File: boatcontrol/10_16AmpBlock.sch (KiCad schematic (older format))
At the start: 15 parts, among them U6101 ULN2803A

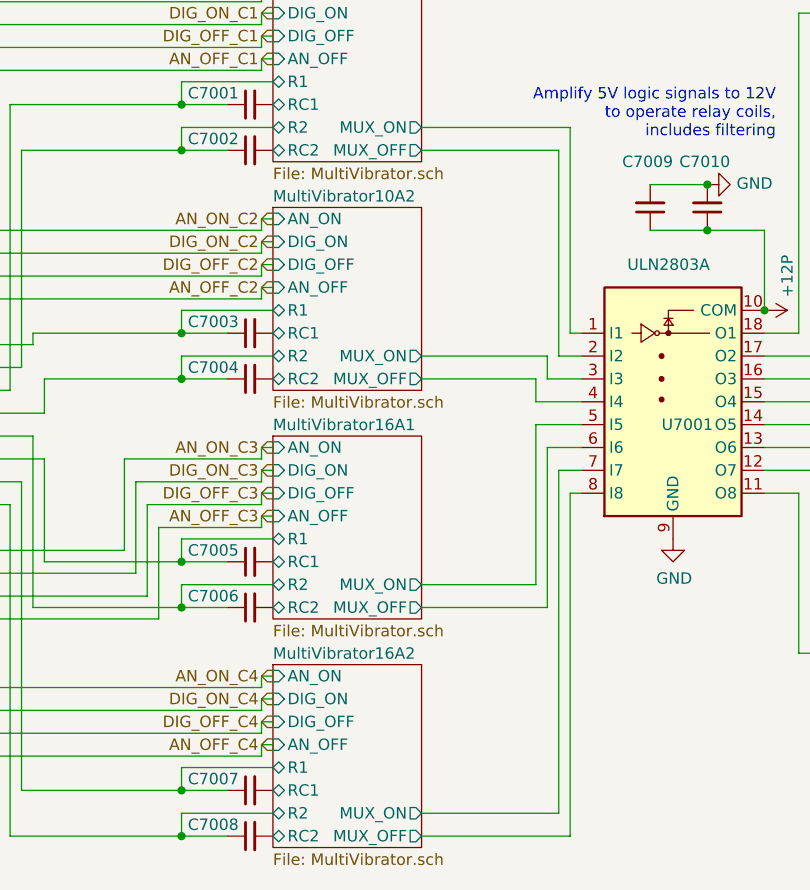
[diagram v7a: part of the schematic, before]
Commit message: Add xors on input
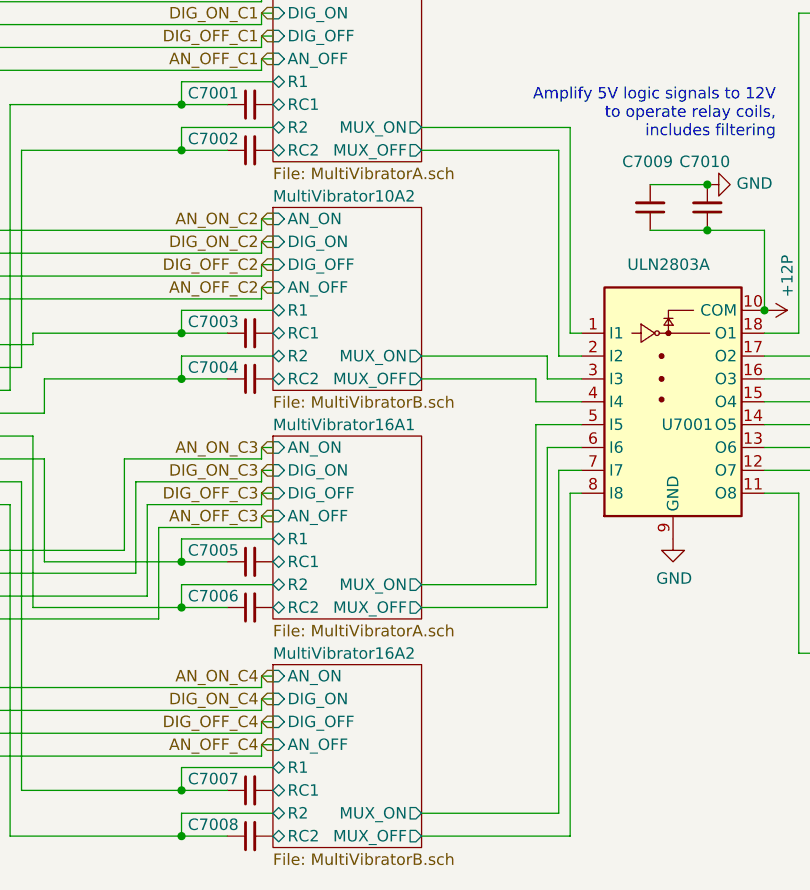
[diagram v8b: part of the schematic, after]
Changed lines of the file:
@@
 U 604747CD
 F0 "MultiVibrator10A1" 50
-F1 "MultiVibrator.sch" 50
+F1 "MultiVibratorA.sch" 50
 F2 "DIG_OFF" I L 4750 2200 50
 F3 "AN_OFF" I L 4750 2300 50
@@
 U 604747E7
 F0 "MultiVibrator10A2" 50
-F1 "MultiVibrator.sch" 50
+F1 "MultiVibratorB.sch" 50
 F2 "DIG_OFF" I L 4750 3200 50
 F3 "AN_OFF" I L 4750 3300 50
@@
 U 604747F3
 F0 "MultiVibrator16A1" 50
-F1 "MultiVibrator.sch" 50
+F1 "MultiVibratorA.sch" 50
 F2 "DIG_OFF" I L 4750 4200 50
 F3 "AN_OFF" I L 4750 4300 50
@@
 U 604747FF
 F0 "MultiVibrator16A2" 50
-F1 "MultiVibrator.sch" 50
+F1 "MultiVibratorB.sch" 50
 F2 "DIG_OFF" I L 4750 5200 50
 F3 "AN_OFF" I L 4750 5300 50
@@
 AR Path="/D16552B4/5FA17F86/602F484F" Ref="#PWR?"  Part="1"
 AR Path="/D1BB8DB4/5F75E923/602F484F" Ref="#PWR?"  Part="1"
+AR Path="/D1BB8DB4/5F76AF55/602F484F" Ref="#PWR?"  Part="1"
 F 0 "#PWR?" H 2450 3400 50  0001 C CNN
 F 1 "+5V" H 2600 3600 50  0000 C CNN
@@
 AR Path="/D16552B4/5FA17F38/602F4855" Ref="#PWR?"  Part="1"
 AR Path="/D1BB8DB4/5F75E923/602F4855" Ref="#PWR?"  Part="1"
+AR Path="/D1BB8DB4/5F76AF55/602F4855" Ref="#PWR?"  Part="1"
 F 0 "#PWR?" H 2450 2400 50  0001 C CNN
 F 1 "GND" H 2300 2600 50  0000 C CNN
@@
 AR Path="/D16552B4/5FA17F38/602F485B" Ref="#PWR?"  Part="1"
 AR Path="/D1BB8DB4/5F75E923/602F485B" Ref="#PWR?"  Part="1"
+AR Path="/D1BB8DB4/5F76AF55/602F485B" Ref="#PWR?"  Part="1"
 F 0 "#PWR?" H 2450 4200 50  0001 C CNN
 F 1 "GND" H 2300 4400 50  0000 C CNN
